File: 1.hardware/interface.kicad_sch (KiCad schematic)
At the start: 36 parts, among them J10 ESP_DBG_CONN, J11 ESP_BOOT_CONN, J4 CAN_CONN, J5 I2C_CONN, J6 CAN_CONN2, J7 EXTRA_SPI3_CONN, J8 USB_C, J9 UART_CONN, U4 SN65HVD230, U5 ESP32-C3-WROOM-02

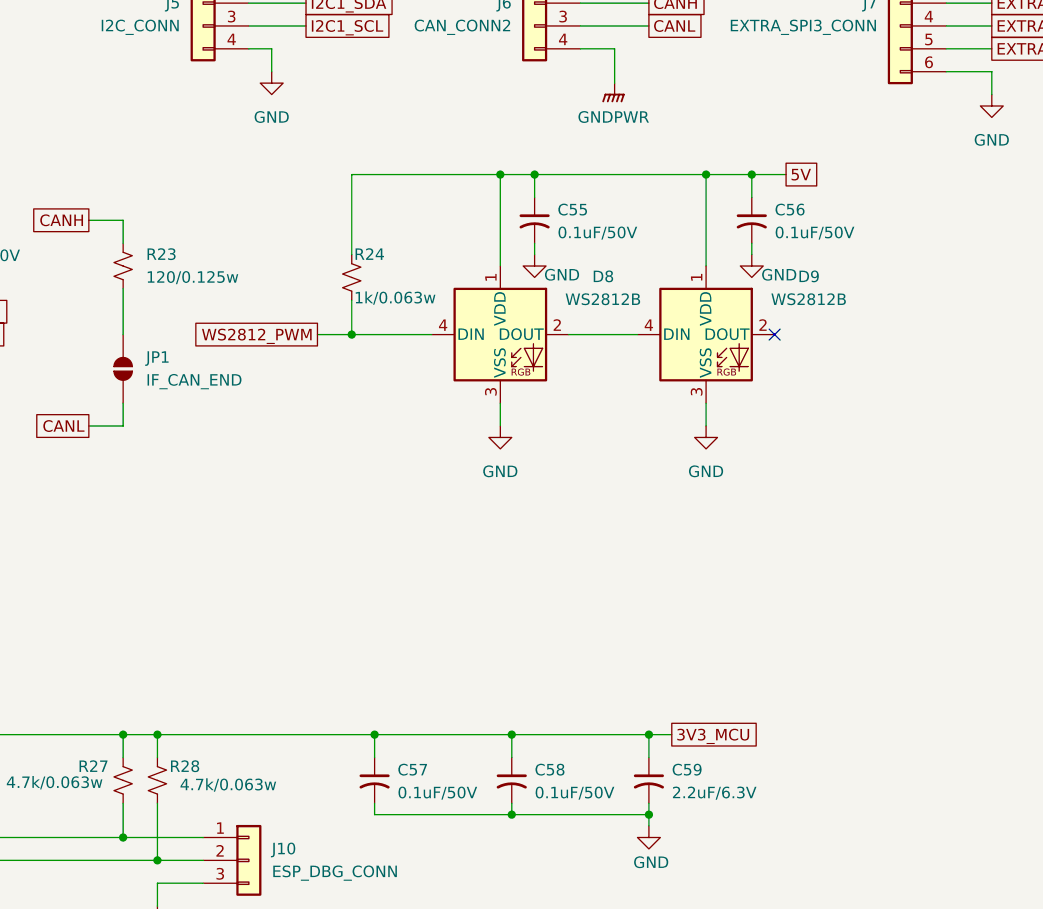
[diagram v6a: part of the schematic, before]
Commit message: 스펙 정함
4층 기판, 비아 0.3 / 0.5 사이즈, 외부 2온즈, Plugger Via, 77달러 정도 나옴
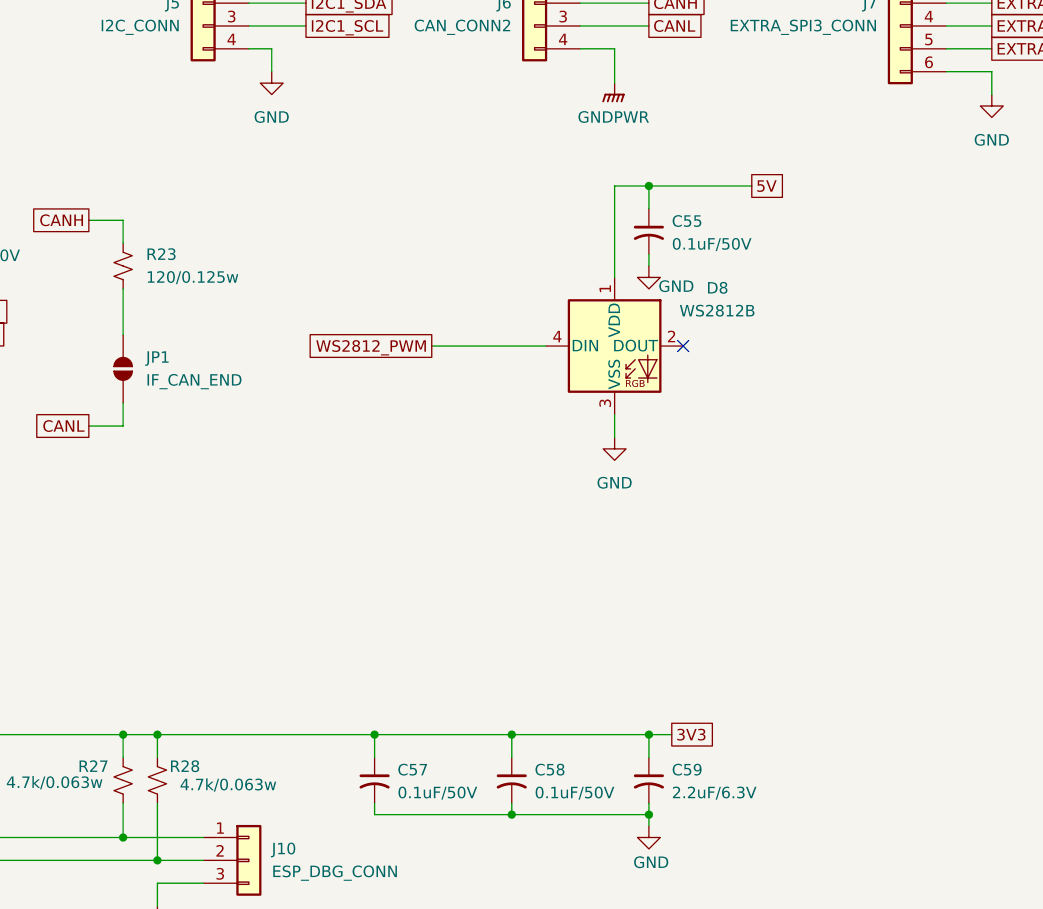
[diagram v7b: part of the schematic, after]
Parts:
- removed C56: 0.1uF/50V, Capacitor_SMD:C_0603_1608Metric, symbol Device:C_Small_US
- removed D9: WS2812B, LED_SMD:LED_WS2812B_PLCC4_5.0x5.0mm_P3.2mm, symbol LED:WS2812B
- removed R24: 1k/0.063w, Resistor_SMD:R_0402_1005Metric, symbol Device:R_Small_US
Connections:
- net 3V3: now also C57.1, C58.1, C59.1, R27.1, R28.1, R29.1, R30.1, U5.1 (3V3)
- net 3V3_MCU: no longer C57.1, C58.1, C59.1, R27.1, R28.1, R29.1, R30.1, U5.1 (3V3)
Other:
- moved on the sheet: C55, D8

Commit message: 오류 일단 다 잡음
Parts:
- removed J7: EXTRA_SPI3_CONN, Connector_PinSocket_2.54mm:PinSocket_1x06_P2.54mm_Vertical, symbol Connector_Generic:Conn_01x06
- C122, C55, C57, C58: footprint Capacitor_SMD:C_0603_1608Metric -> Capacitor_SMD:C_0402_1005Metric
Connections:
- net 3V3: now also R33.2
- net 3V3_MCU: no longer R33.2
